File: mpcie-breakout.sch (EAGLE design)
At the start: 43 parts, among them K1 694108106102, U1 IP4234CZ6, U2 LD1085D2T33R, X1 MPCIE-JAE, X2 MINI-USB-SHIELD-UX60-MB-5ST

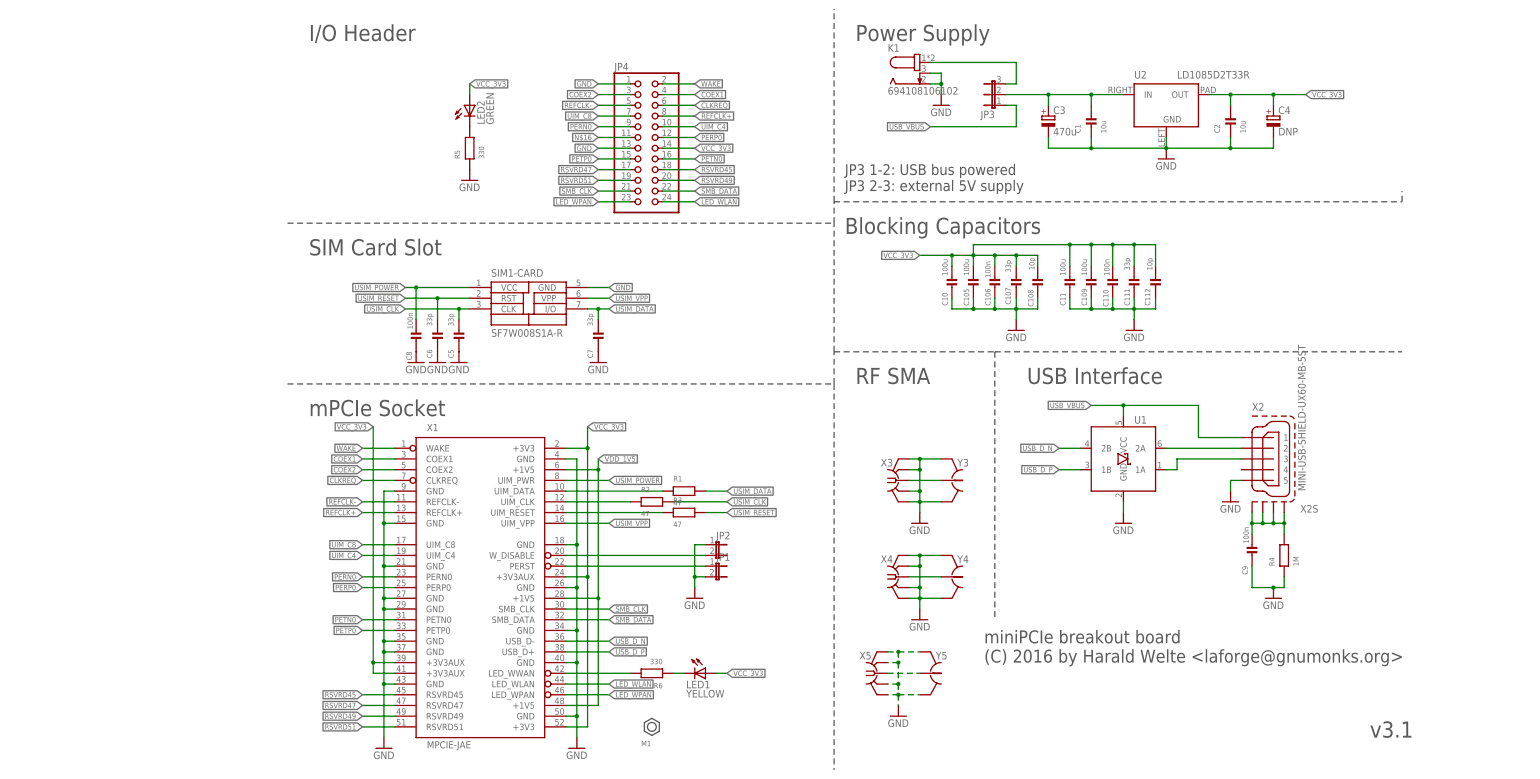
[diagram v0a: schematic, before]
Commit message: pinout defs
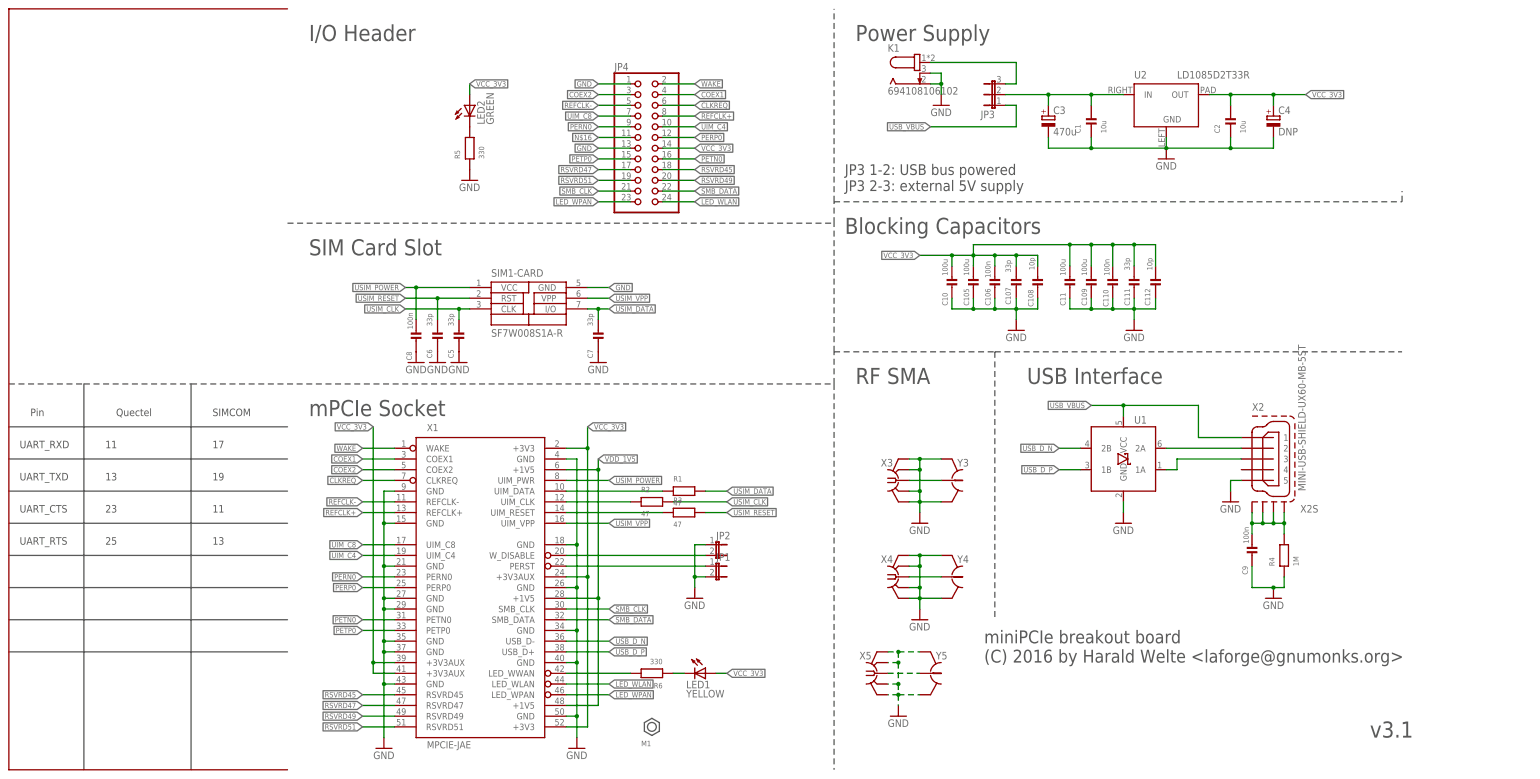
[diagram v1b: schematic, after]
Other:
- note added: "11"
- note added: "13"
- note added: "17"
- note added: "19"
- note added: "23"
- note added: "25"
- note added: "Pin"
- note added: "Quectel"
- note added: "SIMCOM"
- note added: "UART_CTS"
- note added: "UART_RTS"
- note added: "UART_RXD"
- note added: "UART_TXD"
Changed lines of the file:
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@@
 <setting verticaltext="up"/>
 </settings>
-<grid distance="0.1" unitdist="inch" unit="inch" style="lines" multiple="1" display="no" altdistance="0.01" altunitdist="inch" altunit="inch"/>
+<grid distance="0.1" unitdist="inch" unit="inch" style="lines" multiple="1" display="yes" altdistance="0.01" altunitdist="inch" altunit="inch"/>
 <layers>
 <layer number="1" name="Top" color="4" fill="1" visible="no" active="no"/>
@@
 <wire x1="129.54" y1="129.54" x2="129.54" y2="134.62" width="0.1524" layer="97" style="longdash"/>
 <wire x1="129.54" y1="134.62" x2="129.54" y2="180.34" width="0.1524" layer="97" style="longdash"/>
-<wire x1="0" y1="91.44" x2="129.54" y2="91.44" width="0.1524" layer="97" style="longdash"/>
+<wire x1="-66.04" y1="91.44" x2="-48.26" y2="91.44" width="0.1524" layer="97" style="longdash"/>
+<wire x1="-48.26" y1="91.44" x2="-22.86" y2="91.44" width="0.1524" layer="97" style="longdash"/>
+<wire x1="-22.86" y1="91.44" x2="129.54" y2="91.44" width="0.1524" layer="97" style="longdash"/>
 <wire x1="129.54" y1="91.44" x2="129.54" y2="99.06" width="0.1524" layer="97" style="longdash"/>
 <wire x1="129.54" y1="99.06" x2="129.54" y2="129.54" width="0.1524" layer="97" style="longdash"/>
@@
 <wire x1="167.64" y1="99.06" x2="167.64" y2="35.56" width="0.1524" layer="97" style="longdash"/>
 <text x="256.54" y="7.62" size="3.81" layer="97">&gt;VERSION</text>
+<wire x1="0" y1="0" x2="-66.04" y2="0" width="0.2032" layer="94"/>
+<wire x1="-66.04" y1="0" x2="-66.04" y2="180.34" width="0.2032" layer="94"/>
+<wire x1="-66.04" y1="180.34" x2="0" y2="180.34" width="0.2032" layer="94"/>
+<wire x1="0" y1="81.28" x2="-66.04" y2="81.28" width="0.2032" layer="97"/>
+<wire x1="-48.26" y1="91.44" x2="-48.26" y2="0" width="0.2032" layer="97"/>
+<wire x1="-22.86" y1="91.44" x2="-22.86" y2="0" width="0.2032" layer="97"/>
+<text x="-40.64" y="83.82" size="1.778" layer="97">Quectel</text>
+<text x="-17.78" y="83.82" size="1.778" layer="97">SIMCOM</text>
+<text x="-60.96" y="83.82" size="1.778" layer="97">Pin</text>
+<wire x1="0" y1="73.66" x2="-66.04" y2="73.66" width="0.2032" layer="97"/>
+<wire x1="0" y1="66.04" x2="-66.04" y2="66.04" width="0.2032" layer="97"/>
+<wire x1="0" y1="58.42" x2="-66.04" y2="58.42" width="0.2032" layer="97"/>
+<wire x1="0" y1="50.8" x2="-66.04" y2="50.8" width="0.2032" layer="97"/>
+<wire x1="0" y1="43.18" x2="-66.04" y2="43.18" width="0.2032" layer="97"/>
+<wire x1="0" y1="35.56" x2="-66.04" y2="35.56" width="0.2032" layer="97"/>
+<wire x1="0" y1="27.94" x2="-66.04" y2="27.94" width="0.2032" layer="97"/>
+<text x="-63.5" y="76.2" size="1.778" layer="97">UART_RXD</text>
+<text x="-63.5" y="68.58" size="1.778" layer="97">UART_TXD</text>
+<text x="-63.5" y="60.96" size="1.778" layer="97">UART_CTS</text>
+<text x="-63.5" y="53.34" size="1.778" layer="97">UART_RTS</text>
+<text x="-17.78" y="76.2" size="1.778" layer="97">17</text>
+<text x="-17.78" y="68.58" size="1.778" layer="97">19</text>
+<text x="-17.78" y="60.96" size="1.778" layer="97">11</text>
+<text x="-17.78" y="53.34" size="1.778" layer="97">13</text>
+<text x="-43.18" y="76.2" size="1.778" layer="97">11</text>
+<text x="-43.18" y="68.58" size="1.778" layer="97">13</text>
+<text x="-43.18" y="60.96" size="1.778" layer="97">23</text>
+<text x="-43.18" y="53.34" size="1.778" layer="97">25</text>
 </plain>
 <instances>

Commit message: not so easy about UART !
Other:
- note added: "31"
- note added: "UART_DCD"
- note added: "UART_DTR"
- note added: "UART_RI"
- note added: "n.a."
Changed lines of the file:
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@@
 <text x="-43.18" y="60.96" size="1.778" layer="97">23</text>
 <text x="-43.18" y="53.34" size="1.778" layer="97">25</text>
+<text x="-63.5" y="45.72" size="1.778" layer="97">UART_DCD</text>
+<text x="-63.5" y="38.1" size="1.778" layer="97">UART_DTR</text>
+<text x="-63.5" y="30.48" size="1.778" layer="97">UART_RI</text>
+<wire x1="0" y1="20.32" x2="-66.04" y2="20.32" width="0.2032" layer="97"/>
+<text x="-17.78" y="45.72" size="1.778" layer="97">31</text>
+<text x="-17.78" y="38.1" size="1.778" layer="97">23</text>
+<text x="-17.78" y="30.48" size="1.778" layer="97">25</text>
+<text x="-43.18" y="30.48" size="1.778" layer="97">17</text>
+<text x="-43.18" y="38.1" size="1.778" layer="97">31</text>
+<text x="-43.18" y="45.72" size="1.778" layer="97">n.a.</text>
 </plain>
 <instances>

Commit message: Comments about UART.
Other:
- note added: "1"
- note added: "10"
- note added: "12"
- note added: "26"
- note added: "27"
- note added: "5"
- note added: "7"
- note added: "8"
- note added: "9"
- note added: "CTS"
- note added: "ESP32"
- note added: "GND"
- note added: "PERN0"
- note added: "PERP0"
- note added: "REFCLK+"
- note added: "REFCLK-"
- note added: "RTS"
- note added: "RXD"
- note added: "TXD"
- note added: "UIM_C4"
- note added: "UIM_C8"
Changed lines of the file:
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@@
 <wire x1="96.52" y1="43.18" x2="30.48" y2="43.18" width="0.2032" layer="97"/>
 <wire x1="96.52" y1="35.56" x2="30.48" y2="35.56" width="0.2032" layer="97"/>
+<text x="58.42" y="114.3" size="1.778" layer="97">REFCLK-</text>
+<text x="58.42" y="106.68" size="1.778" layer="97">REFCLK+</text>
+<text x="58.42" y="99.06" size="1.778" layer="97">PERN0</text>
+<text x="58.42" y="91.44" size="1.778" layer="97">PERP0</text>
+<text x="83.82" y="99.06" size="1.778" layer="97">REFCLK-</text>
+<text x="83.82" y="91.44" size="1.778" layer="97">REFCLK+</text>
+<text x="83.82" y="106.68" size="1.778" layer="97">UIM_C4</text>
+<text x="83.82" y="114.3" size="1.778" layer="97">UIM_C8</text>
 </plain>
 <instances>
@@
 <plain>
 <text x="30.48" y="101.6" size="3.81" layer="97" font="vector" ratio="12">I/O Header</text>
+<wire x1="215.9" y1="142.24" x2="149.86" y2="142.24" width="0.2032" layer="97"/>
+<wire x1="167.64" y1="152.4" x2="167.64" y2="111.76" width="0.2032" layer="97"/>
+<wire x1="193.04" y1="152.4" x2="193.04" y2="111.76" width="0.2032" layer="97"/>
+<text x="172.72" y="144.78" size="1.778" layer="97">Quectel</text>
+<text x="198.12" y="144.78" size="1.778" layer="97">ESP32</text>
+<text x="154.94" y="144.78" size="1.778" layer="97">Pin</text>
+<wire x1="215.9" y1="134.62" x2="149.86" y2="134.62" width="0.2032" layer="97"/>
+<wire x1="215.9" y1="127" x2="149.86" y2="127" width="0.2032" layer="97"/>
+<wire x1="215.9" y1="119.38" x2="149.86" y2="119.38" width="0.2032" layer="97"/>
+<wire x1="215.9" y1="111.76" x2="193.04" y2="111.76" width="0.2032" layer="97"/>
+<text x="152.4" y="137.16" size="1.778" layer="97">UART_RXD</text>
+<text x="152.4" y="129.54" size="1.778" layer="97">UART_TXD</text>
+<text x="152.4" y="121.92" size="1.778" layer="97">UART_CTS</text>
+<text x="152.4" y="114.3" size="1.778" layer="97">UART_RTS</text>
+<text x="198.12" y="129.54" size="1.778" layer="97">26</text>
+<text x="198.12" y="137.16" size="1.778" layer="97">25</text>
+<text x="198.12" y="114.3" size="1.778" layer="97">23</text>
+<text x="198.12" y="121.92" size="1.778" layer="97">27</text>
+<text x="172.72" y="137.16" size="1.778" layer="97">5</text>
+<text x="172.72" y="129.54" size="1.778" layer="97">8</text>
+<text x="172.72" y="121.92" size="1.778" layer="97">9</text>
+<text x="172.72" y="114.3" size="1.778" layer="97">12</text>
+<wire x1="193.04" y1="111.76" x2="167.64" y2="111.76" width="0.2032" layer="97"/>
+<wire x1="167.64" y1="111.76" x2="149.86" y2="111.76" width="0.2032" layer="97"/>
+<wire x1="215.9" y1="152.4" x2="215.9" y2="111.76" width="0.2032" layer="97"/>
+<wire x1="149.86" y1="152.4" x2="149.86" y2="111.76" width="0.2032" layer="97"/>
+<wire x1="215.9" y1="152.4" x2="149.86" y2="152.4" width="0.2032" layer="97"/>
+<text x="177.8" y="137.16" size="1.778" layer="97">REFCLK-</text>
+<text x="177.8" y="129.54" size="1.778" layer="97">REFCLK+</text>
+<text x="177.8" y="121.92" size="1.778" layer="97">PERN0</text>
+<text x="177.8" y="114.3" size="1.778" layer="97">PERP0</text>
+<wire x1="215.9" y1="104.14" x2="193.04" y2="104.14" width="0.2032" layer="97"/>
+<wire x1="193.04" y1="104.14" x2="167.64" y2="104.14" width="0.2032" layer="97"/>
+<wire x1="167.64" y1="104.14" x2="149.86" y2="104.14" width="0.2032" layer="97"/>
+<wire x1="215.9" y1="111.76" x2="215.9" y2="104.14" width="0.2032" layer="97"/>
+<wire x1="193.04" y1="111.76" x2="193.04" y2="104.14" width="0.2032" layer="97"/>
+<wire x1="167.64" y1="111.76" x2="167.64" y2="104.14" width="0.2032" layer="97"/>
+<wire x1="149.86" y1="111.76" x2="149.86" y2="104.14" width="0.2032" layer="97"/>
+<text x="152.4" y="106.68" size="1.778" layer="97">GND</text>
+<text x="172.72" y="106.68" size="1.778" layer="97">1</text>
+<text x="195.58" y="106.68" size="1.778" layer="97">GND</text>
+<text x="203.2" y="137.16" size="1.778" layer="97">TXD</text>
+<text x="203.2" y="129.54" size="1.778" layer="97">RXD</text>
+<text x="203.2" y="121.92" size="1.778" layer="97">RTS</text>
+<text x="203.2" y="114.3" size="1.778" layer="97">CTS</text>
+<wire x1="215.9" y1="86.36" x2="149.86" y2="86.36" width="0.2032" layer="97"/>
+<wire x1="167.64" y1="96.52" x2="167.64" y2="55.88" width="0.2032" layer="97"/>
+<wire x1="193.04" y1="96.52" x2="193.04" y2="55.88" width="0.2032" layer="97"/>
+<text x="198.12" y="88.9" size="1.778" layer="97">ESP32</text>
+<text x="154.94" y="88.9" size="1.778" layer="97">Pin</text>
+<wire x1="215.9" y1="78.74" x2="149.86" y2="78.74" width="0.2032" layer="97"/>
+<wire x1="215.9" y1="71.12" x2="149.86" y2="71.12" width="0.2032" layer="97"/>
+<wire x1="215.9" y1="63.5" x2="149.86" y2="63.5" width="0.2032" layer="97"/>
+<wire x1="215.9" y1="55.88" x2="193.04" y2="55.88" width="0.2032" layer="97"/>
+<text x="152.4" y="81.28" size="1.778" layer="97">UART_RXD</text>
+<text x="152.4" y="73.66" size="1.778" layer="97">UART_TXD</text>
+<text x="152.4" y="66.04" size="1.778" layer="97">UART_CTS</text>
+<text x="152.4" y="58.42" size="1.778" layer="97">UART_RTS</text>
+<text x="198.12" y="73.66" size="1.778" layer="97">26</text>
+<text x="198.12" y="81.28" size="1.778" layer="97">25</text>
+<text x="198.12" y="58.42" size="1.778" layer="97">23</text>
+<text x="198.12" y="66.04" size="1.778" layer="97">27</text>
+<wire x1="193.04" y1="55.88" x2="167.64" y2="55.88" width="0.2032" layer="97"/>
+<wire x1="167.64" y1="55.88" x2="149.86" y2="55.88" width="0.2032" layer="97"/>
+<wire x1="215.9" y1="96.52" x2="215.9" y2="55.88" width="0.2032" layer="97"/>
+<wire x1="149.86" y1="96.52" x2="149.86" y2="55.88" width="0.2032" layer="97"/>
+<wire x1="215.9" y1="96.52" x2="149.86" y2="96.52" width="0.2032" layer="97"/>
+<wire x1="215.9" y1="48.26" x2="193.04" y2="48.26" width="0.2032" layer="97"/>
+<wire x1="193.04" y1="48.26" x2="167.64" y2="48.26" width="0.2032" layer="97"/>
+<wire x1="167.64" y1="48.26" x2="149.86" y2="48.26" width="0.2032" layer="97"/>
+<wire x1="215.9" y1="55.88" x2="215.9" y2="48.26" width="0.2032" layer="97"/>
+<wire x1="193.04" y1="55.88" x2="193.04" y2="48.26" width="0.2032" layer="97"/>
+<wire x1="167.64" y1="55.88" x2="167.64" y2="48.26" width="0.2032" layer="97"/>
+<wire x1="149.86" y1="55.88" x2="149.86" y2="48.26" width="0.2032" layer="97"/>
+<text x="152.4" y="50.8" size="1.778" layer="97">GND</text>
+<text x="172.72" y="50.8" size="1.778" layer="97">1</text>
+<text x="195.58" y="50.8" size="1.778" layer="97">GND</text>
+<text x="203.2" y="81.28" size="1.778" layer="97">TXD</text>
+<text x="203.2" y="73.66" size="1.778" layer="97">RXD</text>
+<text x="203.2" y="66.04" size="1.778" layer="97">RTS</text>
+<text x="203.2" y="58.42" size="1.778" layer="97">CTS</text>
+<text x="172.72" y="88.9" size="1.778" layer="97">SIMCOM</text>
+<text x="172.72" y="81.28" size="1.778" layer="97">7</text>
+<text x="172.72" y="73.66" size="1.778" layer="97">10</text>
+<text x="172.72" y="66.04" size="1.778" layer="97">5</text>
+<text x="172.72" y="58.42" size="1.778" layer="97">8</text>
+<text x="177.8" y="66.04" size="1.778" layer="97">REFCLK-</text>
+<text x="177.8" y="58.42" size="1.778" layer="97">REFCLK+</text>
+<text x="177.8" y="73.66" size="1.778" layer="97">UIM_C4</text>
+<text x="177.8" y="81.28" size="1.778" layer="97">UIM_C8</text>
 </plain>
 <instances>
@@
 <attribute name="CLASS" x="68.58" y="86.36" size="1.778" layer="96" display="off"/>
 <attribute name="LINK" x="68.58" y="86.36" size="1.778" layer="96" display="off"/>
-<attribute name="NAME" x="72.136" y="81.788" size="1.778" layer="95" rot="R90"/>
-<attribute name="VALUE" x="74.295" y="81.788" size="1.778" layer="96" rot="R90"/>
+<attribute name="NAME" x="62.992" y="89.916" size="1.778" layer="95" rot="R180"/>
+<attribute name="VALUE" x="62.992" y="86.995" size="1.778" layer="96" rot="R180"/>
 </instance>
 <instance part="R5" gate="G$1" x="68.58" y="76.2" smashed="yes" rot="R90">
@@
 <segment>
 <pinref part="LED2" gate="G$1" pin="A"/>
-<wire x1="68.58" y1="88.9" x2="68.58" y2="91.44" width="0.1524" layer="91"/>
-<label x="68.58" y="91.44" size="1.27" layer="95" xref="yes"/>
-</segment>
-</net>
+<wire x1="68.58" y1="88.9" x2="68.58" y2="99.06" width="0.1524" layer="91"/>
+<label x="68.58" y="99.06" size="1.27" layer="95" xref="yes"/>
+</segment>
+</net>

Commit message: gitflow-feature-stash: nanoSIM
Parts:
- removed SIM1: SF7W008S1A-R, SF7W008S1A-SIM:SF7W008S1A-R
- removed X3, X4, X5: (no value), laforge:SMA-F-S-TH
- removed Y3, Y4, Y5: (no value), laforge:HRS_UFL
- added J1: 693043020611, Wurth_Connectors_WR-CRD:693043020611
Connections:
- removed net N$13: X3.1, Y3.1
- removed net N$14: X4.1, Y4.1
- removed net N$7: X5.1, Y5.1
- net GND: now also J1.GND, J1.SHIELD; no longer SIM1-CARD.GND, X3.GND@1, X3.GND@2, X3.GND@3, X3.GND@4, X4.GND@1, X4.GND@2, X4.GND@3, X4.GND@4, X5.GND@1, X5.GND@2, X5.GND@3, X5.GND@4, Y3.GND@1, Y3.GND@2, Y4.GND@1, Y4.GND@2, Y5.GND@1, Y5.GND@2
- net USIM_CLK: now also J1.CLK; no longer SIM1-CARD.CLK
- net USIM_DATA: now also J1.I/O; no longer SIM1-CARD.I/O
- net USIM_POWER: now also J1.VCC; no longer SIM1-CARD.VCC
- net USIM_RESET: now also J1.RST; no longer SIM1-CARD.RST
- net USIM_VPP: now also J1.VPP; no longer SIM1-CARD.VPP
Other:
- note removed: "RF SMA"
